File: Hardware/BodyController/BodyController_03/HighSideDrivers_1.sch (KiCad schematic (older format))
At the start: 44 parts, among them Q8 2N7002, Q9 2N7002, U4 BTS716G, U5 BTS500801TMAATMA1, U6 BTS500801TMAATMA1, U7 BTS50202EKAXUMA2, U8 BTS50202EKAXUMA2, U9 BTS50202EKAXUMA2

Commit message: Updated layout, cleaned up directory, and modified BOM
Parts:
- Q8, Q9: symbol 2N7002 -> 2N7002-RESCUE-BodyController_03
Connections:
- net AUX_PORT_EN: now also Q8.1 (G)
- net HORN_EN: now also Q9.1 (G)
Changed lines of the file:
@@
 EESchema Schematic File Version 2
+LIBS:BodyController_03-rescue
 LIBS:power
 LIBS:device
@@
 LIBS:contrib
 LIBS:valves
-LIBS:HSD
-LIBS:micros
-LIBS:ICs
-LIBS:Connectors
 LIBS:BodyController_03-cache
 EELAYER 25 0
@@
 $EndComp
 $Comp
-L 2N7002 Q8
+L 2N7002-RESCUE-BodyController_03 Q8
 U 1 1 598C3B55
 P 1850 1700
+AR Path="/598C3B55" Ref="Q8"  Part="1"
+AR Path="/5986882A/59868A89/598C3B55" Ref="Q8"  Part="1"
 F 0 "Q8" H 2050 1775 50  0000 L CNN
 F 1 "2N7002" H 2050 1700 50  0000 L CNN
@@
 $EndComp
 $Comp
-L 2N7002 Q9
+L 2N7002-RESCUE-BodyController_03 Q9
 U 1 1 59907841
 P 1850 3500
+AR Path="/59907841" Ref="Q9"  Part="1"
+AR Path="/5986882A/59868A89/59907841" Ref="Q9"  Part="1"
 F 0 "Q9" H 2050 3575 50  0000 L CNN
 F 1 "2N7002" H 2050 3500 50  0000 L CNN

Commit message: started serious layout
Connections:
- net GND: now also U4.6 (GND3/4)
- net AUX_PORT_ISENSE renamed AUX_PORT_ISENSE_AI
- net HEADLIGHT_ISENSE renamed HEADLIGHT_ISENSE_AI
- net HEATER_ISENSE renamed HEATER_ISENSE_AI
- net HORN_ISENSE renamed HORN_ISENSE_AI
- net TAILLIGHT_ISENSE renamed TAILLIGHT_ISENSE_AI
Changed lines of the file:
@@
 EESchema Schematic File Version 2
-LIBS:BodyController_03-rescue
 LIBS:power
 LIBS:device
@@
 LIBS:contrib
 LIBS:valves
+LIBS:HSD
+LIBS:micros
+LIBS:ICs
+LIBS:Connectors
 LIBS:BodyController_03-cache
 EELAYER 25 0
@@
 $Descr A4 11693 8268
 encoding utf-8
-Sheet 5 11
+Sheet 5 12
 Title ""
 Date ""
@@
 $EndComp
 $Comp
-L +12V #PWR049
+L +12V #PWR039
 U 1 1 598C3AA5
 P 3300 950
-F 0 "#PWR049" H 3300 800 50  0001 C CNN
+F 0 "#PWR039" H 3300 800 50  0001 C CNN
 F 1 "+12V" H 3300 1090 50  0000 C CNN
 F 2 "" H 3300 950 50  0001 C CNN
@@
 $EndComp
 $Comp
-L GND #PWR050
+L GND #PWR040
 U 1 1 598C3BDD
 P 1950 2150
-F 0 "#PWR050" H 1950 1900 50  0001 C CNN
+F 0 "#PWR040" H 1950 1900 50  0001 C CNN
 F 1 "GND" H 1950 2000 50  0000 C CNN
 F 2 "" H 1950 2150 50  0001 C CNN
@@
 $EndComp
 $Comp
-L GND #PWR051
+L GND #PWR041
 U 1 1 598C3D0E
 P 3600 2150
-F 0 "#PWR051" H 3600 1900 50  0001 C CNN
+F 0 "#PWR041" H 3600 1900 50  0001 C CNN
 F 1 "GND" H 3600 2000 50  0000 C CNN
 F 2 "" H 3600 2150 50  0001 C CNN
@@
 $EndComp
 $Comp
-L GND #PWR052
+L GND #PWR042
 U 1 1 598C3E06
 P 3100 2150
-F 0 "#PWR052" H 3100 1900 50  0001 C CNN
+F 0 "#PWR042" H 3100 1900 50  0001 C CNN
 F 1 "GND" H 3100 2000 50  0000 C CNN
 F 2 "" H 3100 2150 50  0001 C CNN
@@
 $EndComp
 $Comp
-L GND #PWR053
+L GND #PWR043
 U 1 1 598C3E7D
 P 1550 2150
-F 0 "#PWR053" H 1550 1900 50  0001 C CNN
+F 0 "#PWR043" H 1550 1900 50  0001 C CNN
 F 1 "GND" H 1550 2000 50  0000 C CNN
 F 2 "" H 1550 2150 50  0001 C CNN
@@
 $EndComp
 $Comp
-L GND #PWR054
+L GND #PWR044
 U 1 1 598F4929
 P 8350 4250
-F 0 "#PWR054" H 8350 4000 50  0001 C CNN
+F 0 "#PWR044" H 8350 4000 50  0001 C CNN
 F 1 "GND" H 8350 4100 50  0000 C CNN
 F 2 "" H 8350 4250 50  0001 C CNN
@@
 $EndComp
 $Comp
-L GND #PWR055
+L GND #PWR045
 U 1 1 598F4E19
 P 8050 4050
-F 0 "#PWR055" H 8050 3800 50  0001 C CNN
+F 0 "#PWR045" H 8050 3800 50  0001 C CNN
 F 1 "GND" H 8050 3900 50  0000 C CNN
 F 2 "" H 8050 4050 50  0001 C CNN
@@
 $EndComp
 $Comp
-L GND #PWR056
+L GND #PWR046
 U 1 1 598F4F8A
 P 7500 4050
-F 0 "#PWR056" H 7500 3800 50  0001 C CNN
+F 0 "#PWR046" H 7500 3800 50  0001 C CNN
 F 1 "GND" H 7500 3900 50  0000 C CNN
 F 2 "" H 7500 4050 50  0001 C CNN
@@
 $EndComp
 $Comp
-L +12V #PWR057
+L +12V #PWR047
 U 1 1 598F50F5
 P 10150 2800
-F 0 "#PWR057" H 10150 2650 50  0001 C CNN
+F 0 "#PWR047" H 10150 2650 50  0001 C CNN
 F 1 "+12V" H 10150 2940 50  0000 C CNN
 F 2 "" H 10150 2800 50  0001 C CNN
@@
 $EndComp
 $Comp
-L +12V #PWR058
+L +12V #PWR048
 U 1 1 598FF533
 P 3500 6050
-F 0 "#PWR058" H 3500 5900 50  0001 C CNN
+F 0 "#PWR048" H 3500 5900 50  0001 C CNN
 F 1 "+12V" H 3500 6190 50  0000 C CNN
 F 2 "" H 3500 6050 50  0001 C CNN
@@
 $EndComp
 $Comp
-L GND #PWR059
+L GND #PWR049
 U 1 1 59900ED2
 P 3400 7500
-F 0 "#PWR059" H 3400 7250 50  0001 C CNN
+F 0 "#PWR049" H 3400 7250 50  0001 C CNN
 F 1 "GND" H 3400 7350 50  0000 C CNN
 F 2 "" H 3400 7500 50  0001 C CNN
@@
 $EndComp
 $Comp
-L GND #PWR060
+L GND #PWR050
 U 1 1 59902B7E
 P 8350 6350
-F 0 "#PWR060" H 8350 6100 50  0001 C CNN
+F 0 "#PWR050" H 8350 6100 50  0001 C CNN
 F 1 "GND" H 8350 6200 50  0000 C CNN
 F 2 "" H 8350 6350 50  0001 C CNN
@@
 $EndComp
 $Comp
-L GND #PWR061
+L GND #PWR051
 U 1 1 59902BA8
 P 8050 6150
-F 0 "#PWR061" H 8050 5900 50  0001 C CNN
+F 0 "#PWR051" H 8050 5900 50  0001 C CNN
 F 1 "GND" H 8050 6000 50  0000 C CNN
 F 2 "" H 8050 6150 50  0001 C CNN
@@
 $EndComp
 $Comp
-L GND #PWR062
+L GND #PWR052
 U 1 1 59902BB4
 P 7500 6150
-F 0 "#PWR062" H 7500 5900 50  0001 C CNN
+F 0 "#PWR052" H 7500 5900 50  0001 C CNN
 F 1 "GND" H 7500 6000 50  0000 C CNN
 F 2 "" H 7500 6150 50  0001 C CNN
@@
 $EndComp
 $Comp
-L +12V #PWR063
+L +12V #PWR053
 U 1 1 59902BBA
 P 10150 4900
-F 0 "#PWR063" H 10150 4750 50  0001 C CNN
+F 0 "#PWR053" H 10150 4750 50  0001 C CNN
 F 1 "+12V" H 10150 5040 50  0000 C CNN
 F 2 "" H 10150 4900 50  0001 C CNN
@@
 $EndComp
 $Comp
-L GND #PWR064
+L GND #PWR054
 U 1 1 59903F5B
 P 8350 2300
-F 0 "#PWR064" H 8350 2050 50  0001 C CNN
+F 0 "#PWR054" H 8350 2050 50  0001 C CNN
 F 1 "GND" H 8350 2150 50  0000 C CNN
 F 2 "" H 8350 2300 50  0001 C CNN
@@
 $EndComp
 $Comp
-L GND #PWR065
+L GND #PWR055
 U 1 1 59903F85
 P 8050 2100
-F 0 "#PWR065" H 8050 1850 50  0001 C CNN
+F 0 "#PWR055" H 8050 1850 50  0001 C CNN
 F 1 "GND" H 8050 1950 50  0000 C CNN
 F 2 "" H 8050 2100 50  0001 C CNN
@@
 $EndComp
 $Comp
-L GND #PWR066
+L GND #PWR056
 U 1 1 59903F91
 P 7500 2100
-F 0 "#PWR066" H 7500 1850 50  0001 C CNN
+F 0 "#PWR056" H 7500 1850 50  0001 C CNN
 F 1 "GND" H 7500 1950 50  0000 C CNN
 F 2 "" H 7500 2100 50  0001 C CNN
@@
 $EndComp
 $Comp
-L +12V #PWR067
+L +12V #PWR057
 U 1 1 59903F97
 P 10150 850
-F 0 "#PWR067" H 10150 700 50  0001 C CNN
+F 0 "#PWR057" H 10150 700 50  0001 C CNN
 F 1 "+12V" H 10150 990 50  0000 C CNN
 F 2 "" H 10150 850 50  0001 C CNN
@@
 $EndComp
 $Comp
-L +12V #PWR068
+L +12V #PWR058
 U 1 1 5990783B
 P 3300 2750
-F 0 "#PWR068" H 3300 2600 50  0001 C CNN
+F 0 "#PWR058" H 3300 2600 50  0001 C CNN
 F 1 "+12V" H 3300 2890 50  0000 C CNN
 F 2 "" H 3300 2750 50  0001 C CNN
@@
 $EndComp
 $Comp
-L GND #PWR069
+L GND #PWR059
 U 1 1 59907847
 P 1950 3950
-F 0 "#PWR069" H 1950 3700 50  0001 C CNN
+F 0 "#PWR059" H 1950 3700 50  0001 C CNN
 F 1 "GND" H 1950 3800 50  0000 C CNN
 F 2 "" H 1950 3950 50  0001 C CNN
@@
 $EndComp
 $Comp
-L GND #PWR070
+L GND #PWR060
 U 1 1 59907859
 P 3600 3950
-F 0 "#PWR070" H 3600 3700 50  0001 C CNN
+F 0 "#PWR060" H 3600 3700 50  0001 C CNN
 F 1 "GND" H 3600 3800 50  0000 C CNN
 F 2 "" H 3600 3950 50  0001 C CNN
@@
 $EndComp
 $Comp
-L GND #PWR071
+L GND #PWR061
 U 1 1 59907865
 P 3100 3950
-F 0 "#PWR071" H 3100 3700 50  0001 C CNN
+F 0 "#PWR061" H 3100 3700 50  0001 C CNN
 F 1 "GND" H 3100 3800 50  0000 C CNN
 F 2 "" H 3100 3950 50  0001 C CNN
@@
 $EndComp
 $Comp
-L GND #PWR072
+L GND #PWR062
 U 1 1 59907871
 P 1550 3950
-F 0 "#PWR072" H 1550 3700 50  0001 C CNN
+F 0 "#PWR062" H 1550 3700 50  0001 C CNN
 F 1 "GND" H 1550 3800 50  0000 C CNN
 F 2 "" H 1550 3950 50  0001 C CNN
@@
 $EndComp
 $Comp
-L GND #PWR073
+L GND #PWR063
 U 1 1 59908757
 P 5100 3400
-F 0 "#PWR073" H 5100 3150 50  0001 C CNN
+F 0 "#PWR063" H 5100 3150 50  0001 C CNN
 F 1 "GND" H 5100 3250 50  0000 C CNN
 F 2 "" H 5100 3400 50  0001 C CNN
@@
 AUX_PORT_EN
 Text GLabel 3000 1550 0    59   Output ~ 0
-AUX_PORT_ISENSE
+AUX_PORT_ISENSE_AI
 Text Notes 1950 1100 0    59   ~ 0
 AUX PORT OUTPUT\n10A Rated Current\nEfuse 100A
@@
 DIAG_EN
 Text GLabel 7400 3600 0    59   Output ~ 0
-HEADLIGHT_ISENSE
+HEADLIGHT_ISENSE_AI
 Text GLabel 10300 3400 2    59   Output ~ 0
 HEADLIGHT_HI_OUT
@@
 DIAG_EN
 Text GLabel 7400 5700 0    59   Output ~ 0
-HEATER_ISENSE
+HEATER_ISENSE_AI
 Text GLabel 10300 5500 2    59   Output ~ 0
 HEATED_GRIPS_OUT
@@
 DIAG_EN
 Text GLabel 7400 1650 0    59   Output ~ 0
-TAILLIGHT_ISENSE
+TAILLIGHT_ISENSE_AI
 Text GLabel 10300 1450 2    59   Output ~ 0
 TAILLIGHT_OUT
@@
 HORN_EN
 Text GLabel 3000 3350 0    59   Output ~ 0
-HORN_ISENSE
+HORN_ISENSE_AI
 Text Notes 1950 2900 0    59   ~ 0
 HORN OUTPUT\n10A Rated Current\nEfuse 100A
@@
 Connection ~ 4250 6050
 Connection ~ 4350 6050
+Connection ~ 3400 7350
 $EndSCHEMATC

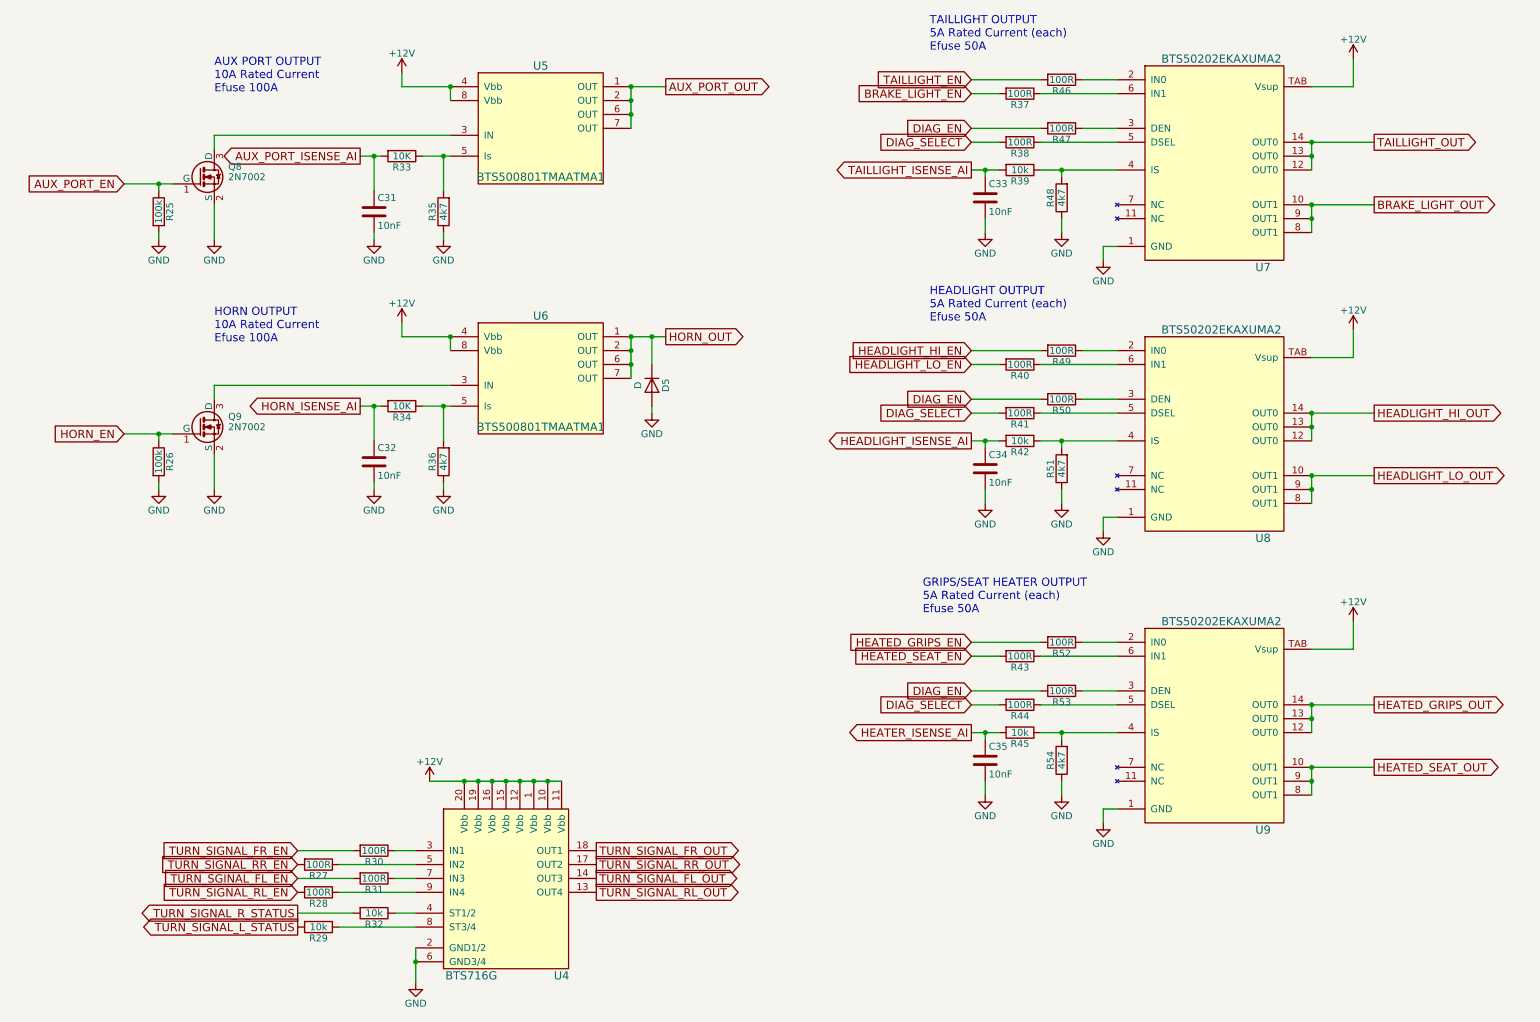
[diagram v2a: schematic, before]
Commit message: Body Controller Layout Done
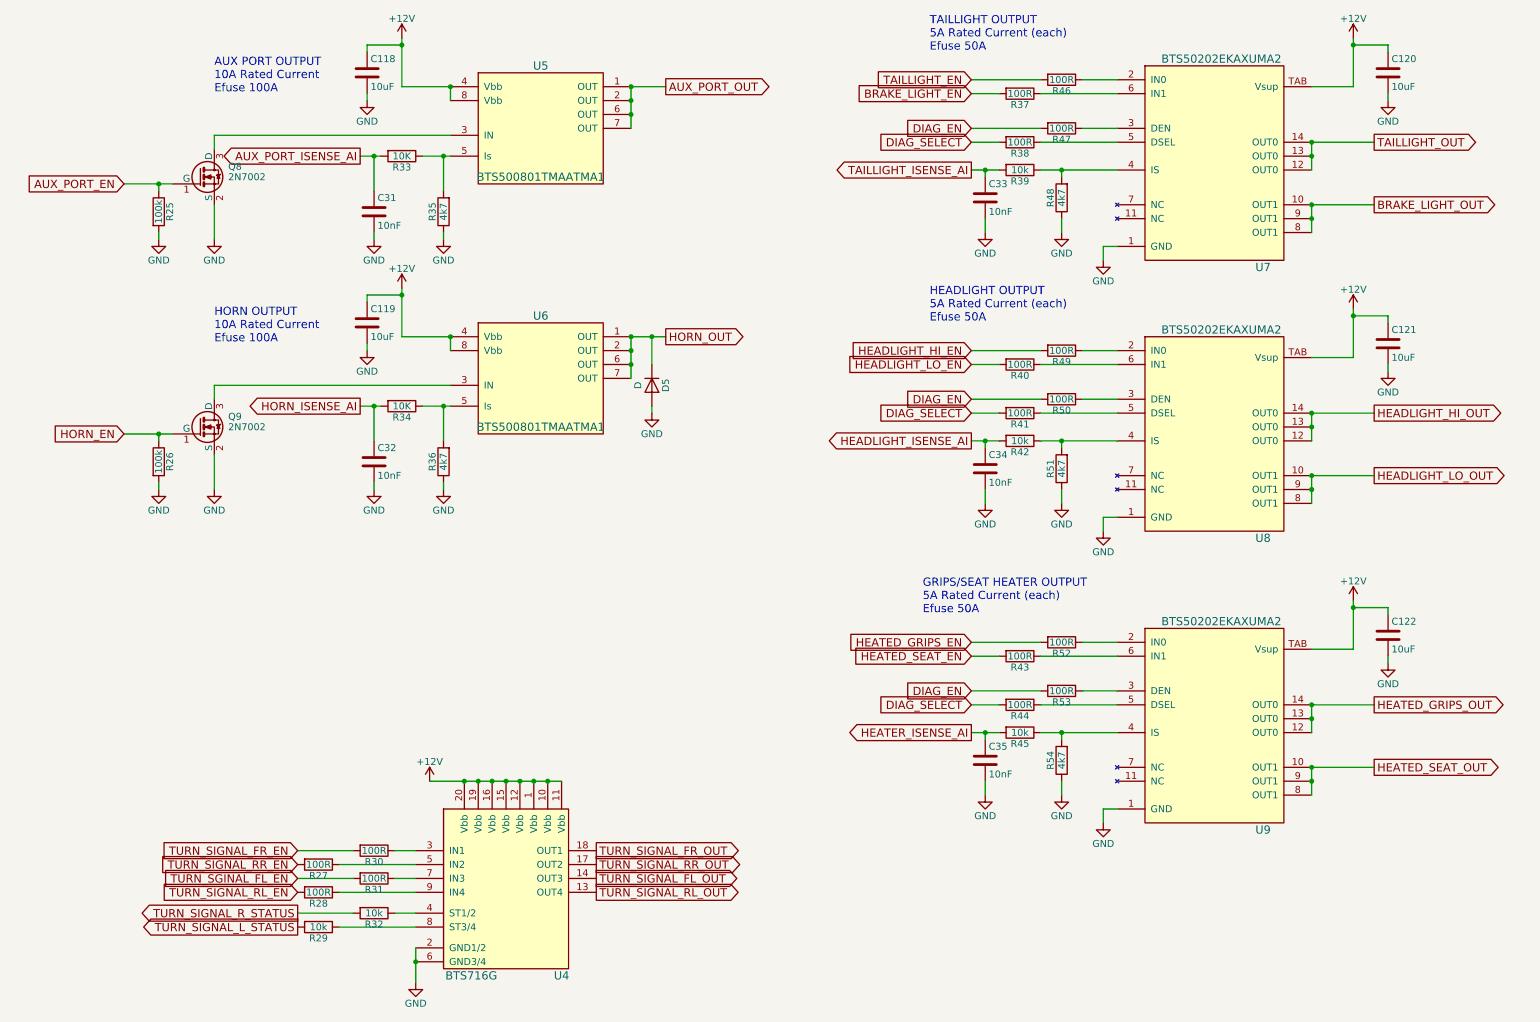
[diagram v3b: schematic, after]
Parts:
- added C118, C119, C120, C121, C122: 10uF, Capacitors_SMD:C_1206, symbol C
- D5: footprint Diodes_SMD:D_SMB -> Footprints:SOT1289; PartNumber S3AB -> PMEG060V100EPDZ
- U5, U6: PartNumber (none) -> BTS500801TMAATMA1
- U7, U8, U9: PartNumber (none) -> BTS50202EKAXUMA2
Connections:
- net +12V: now also C118.1, C119.1, C120.1, C121.1, C122.1
- net GND: now also C118.2, C119.2, C120.2, C121.2, C122.2

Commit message: Added resistor values via BOM importer. Changed layout file to add large CAN resistors and buffer to 1.65V Reference
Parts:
- R25, R26: PartNumber (none) -> AC0603FR-07100KL
- R27, R28, R30, R31, R37, R38, R40, R41, R43, R44, R46, R47, R49, R50, R52, R53: PartNumber (none) -> AC0603FR-07100RL
- R29, R32, R33, R34, R39, R42, R45: PartNumber (none) -> AC0603FR-0710KL
- R35, R36, R48, R51, R54: PartNumber (none) -> AC0603FR-074K7L
